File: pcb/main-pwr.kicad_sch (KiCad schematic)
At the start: 7 parts

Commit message: bom
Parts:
- C2: Part Description (none) -> CAP CER 0.1UF 16V X7R 0402
- R3, R5: Part Description (none) -> RES 10 OHM 1% 1/16W 0402
- R4: Part Description (none) -> WSKW0612 .003 1% EA E3
- R6, R7: footprint library:R_0402_1005Metric -> Resistor_SMD:R_0402_1005Metric; Manufacturer YAGEO -> Vishay Dale; Manufacturer Product Number RC0402FR-07100KL -> CRCW0402100KFKED; Part Description (none) -> RES 100K OHM 1% 1/16W 0402
- R8: renamed from R29; footprint library:R_0402_1005Metric -> Resistor_SMD:R_0402_1005Metric; Manufacturer YAGEO -> Vishay Dale; Manufacturer Product Number RC0402FR-07100KL -> CRCW0402100KFKED; Part Description (none) -> RES 100K OHM 1% 1/16W 0402
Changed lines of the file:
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@@
+			)
+		)
+		(property "Part Description" "RES 10 OHM 1% 1/16W 0402"
+			(at 45.72 31.75 0)
+			(effects
+				(font
+					(size 1.27 1.27)
+				)
+				(hide yes)
 			)
 		)
@@
 			)
 		)
-		(property "Footprint" "library:R_0402_1005Metric"
+		(property "Footprint" "Resistor_SMD:R_0402_1005Metric"
 			(at 128.524 62.484 90)
 			(effects
@@
 			)
 		)
-		(property "Manufacturer" "YAGEO"
+		(property "Manufacturer" "Vishay Dale"
 			(at 128.27 63.5 0)
 			(effects
@@
 			)
 		)
-		(property "Manufacturer Product Number" "RC0402FR-07100KL"
+		(property "Manufacturer Product Number" "CRCW0402100KFKED"
+			(at 128.27 63.5 90)
+			(effects
+				(font
+					(size 1.27 1.27)
+				)
+				(hide yes)
+			)
+		)
+		(property "Part Description" "RES 100K OHM 1% 1/16W 0402"
 			(at 128.27 63.5 90)
 			(effects
@@
 		(dnp no)
 		(fields_autoplaced yes)
-		(property "Reference" "R29"
+		(property "Reference" "R8"
 			(at 128.27 135.89 90)
 			(effects
@@
 			)
 		)
-		(property "Footprint" "library:R_0402_1005Metric"
+		(property "Footprint" "Resistor_SMD:R_0402_1005Metric"
 			(at 128.524 141.224 90)
 			(effects
@@
 			)
 		)
-		(property "Manufacturer" "YAGEO"
+		(property "Manufacturer" "Vishay Dale"
 			(at 128.27 142.24 0)
 			(effects
@@
 			)
 		)
-		(property "Manufacturer Product Number" "RC0402FR-07100KL"
+		(property "Manufacturer Product Number" "CRCW0402100KFKED"
+			(at 128.27 142.24 90)
+			(effects
+				(font
+					(size 1.27 1.27)
+				)
+				(hide yes)
+			)
+		)
+		(property "Part Description" "RES 100K OHM 1% 1/16W 0402"
 			(at 128.27 142.24 90)
 			(effects
@@
 			(project "RPi-HwAB-1"
 				(path "/e63e39d7-6ac0-4ffd-8aa3-1841a4541b55/f9ebb56c-78c7-42ac-bc19-ccbf788f5318"
-					(reference "R29")
+					(reference "R8")
 					(unit 1)
 				)
@@
 			)
 		)
+		(property "Part Description" "WSKW0612 .003 1% EA E3"
+			(at 39.37 25.4 90)
+			(effects
+				(font
+					(size 1.27 1.27)
+				)
+				(hide yes)
+			)
+		)
 		(pin "1"
 		)
@@
 		)
 		(property "Name" ""
+			(at 33.02 31.75 0)
+			(effects
+				(font
+					(size 1.27 1.27)
+				)
+				(hide yes)
+			)
+		)
+		(property "Part Description" "RES 10 OHM 1% 1/16W 0402"
 			(at 33.02 31.75 0)
 			(effects
@@
 			)
 		)
-		(property "Footprint" "library:R_0402_1005Metric"
+		(property "Footprint" "Resistor_SMD:R_0402_1005Metric"
 			(at 128.524 92.964 90)
 			(effects
@@
 			)
 		)
-		(property "Manufacturer" "YAGEO"
+		(property "Manufacturer" "Vishay Dale"
 			(at 128.27 93.98 0)
 			(effects
@@
 			)
 		)
-		(property "Manufacturer Product Number" "RC0402FR-07100KL"
+		(property "Manufacturer Product Number" "CRCW0402100KFKED"
+			(at 128.27 93.98 90)
+			(effects
+				(font
+					(size 1.27 1.27)
+				)
+				(hide yes)
+			)
+		)
+		(property "Part Description" "RES 100K OHM 1% 1/16W 0402"
 			(at 128.27 93.98 90)
 			(effects
@@
 			(at 39.37 40.64 90)
 			(effects
+				(font
+					(size 1.27 1.27)
+				)
+				(hide yes)
+			)
+		)
+		(property "Part Description" "CAP CER 0.1UF 16V X7R 0402"
+			(at 39.37 40.64 90)
+			(effects

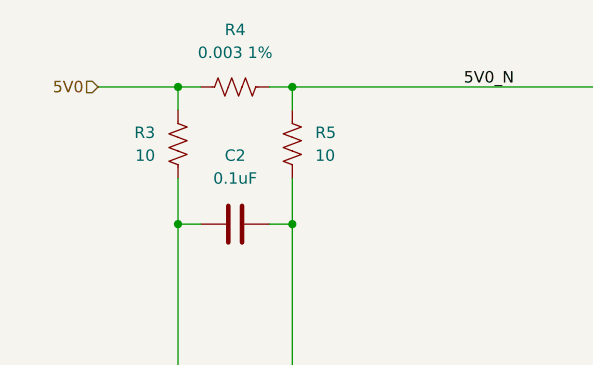
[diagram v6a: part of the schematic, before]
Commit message: added mig ddr pinout constraints
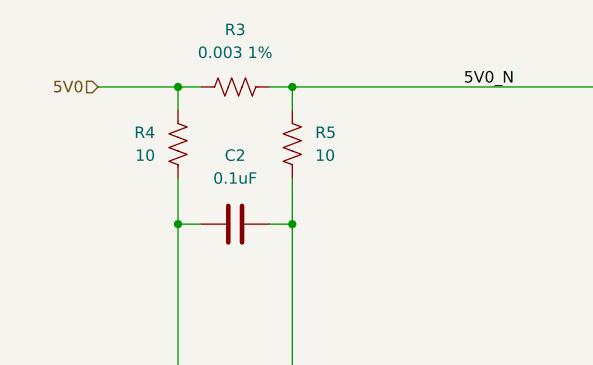
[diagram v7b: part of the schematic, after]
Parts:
- renumbered R4 to R3, R3 to R4
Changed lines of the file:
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@@
 		(dnp no)
 		(fields_autoplaced yes)
-		(property "Reference" "R4"
+		(property "Reference" "R3"
 			(at 39.37 19.05 90)
 			(effects
@@
 			(project ""
 				(path "/e63e39d7-6ac0-4ffd-8aa3-1841a4541b55/f9ebb56c-78c7-42ac-bc19-ccbf788f5318"
-					(reference "R4")
+					(reference "R3")
 					(unit 1)
 				)
@@
 		(on_board yes)
 		(dnp no)
-		(property "Reference" "R3"
+		(property "Reference" "R4"
 			(at 30.48 30.48 0)
 			(effects
@@
 			(project ""
 				(path "/e63e39d7-6ac0-4ffd-8aa3-1841a4541b55/f9ebb56c-78c7-42ac-bc19-ccbf788f5318"
-					(reference "R3")
+					(reference "R4")
 					(unit 1)
 				)

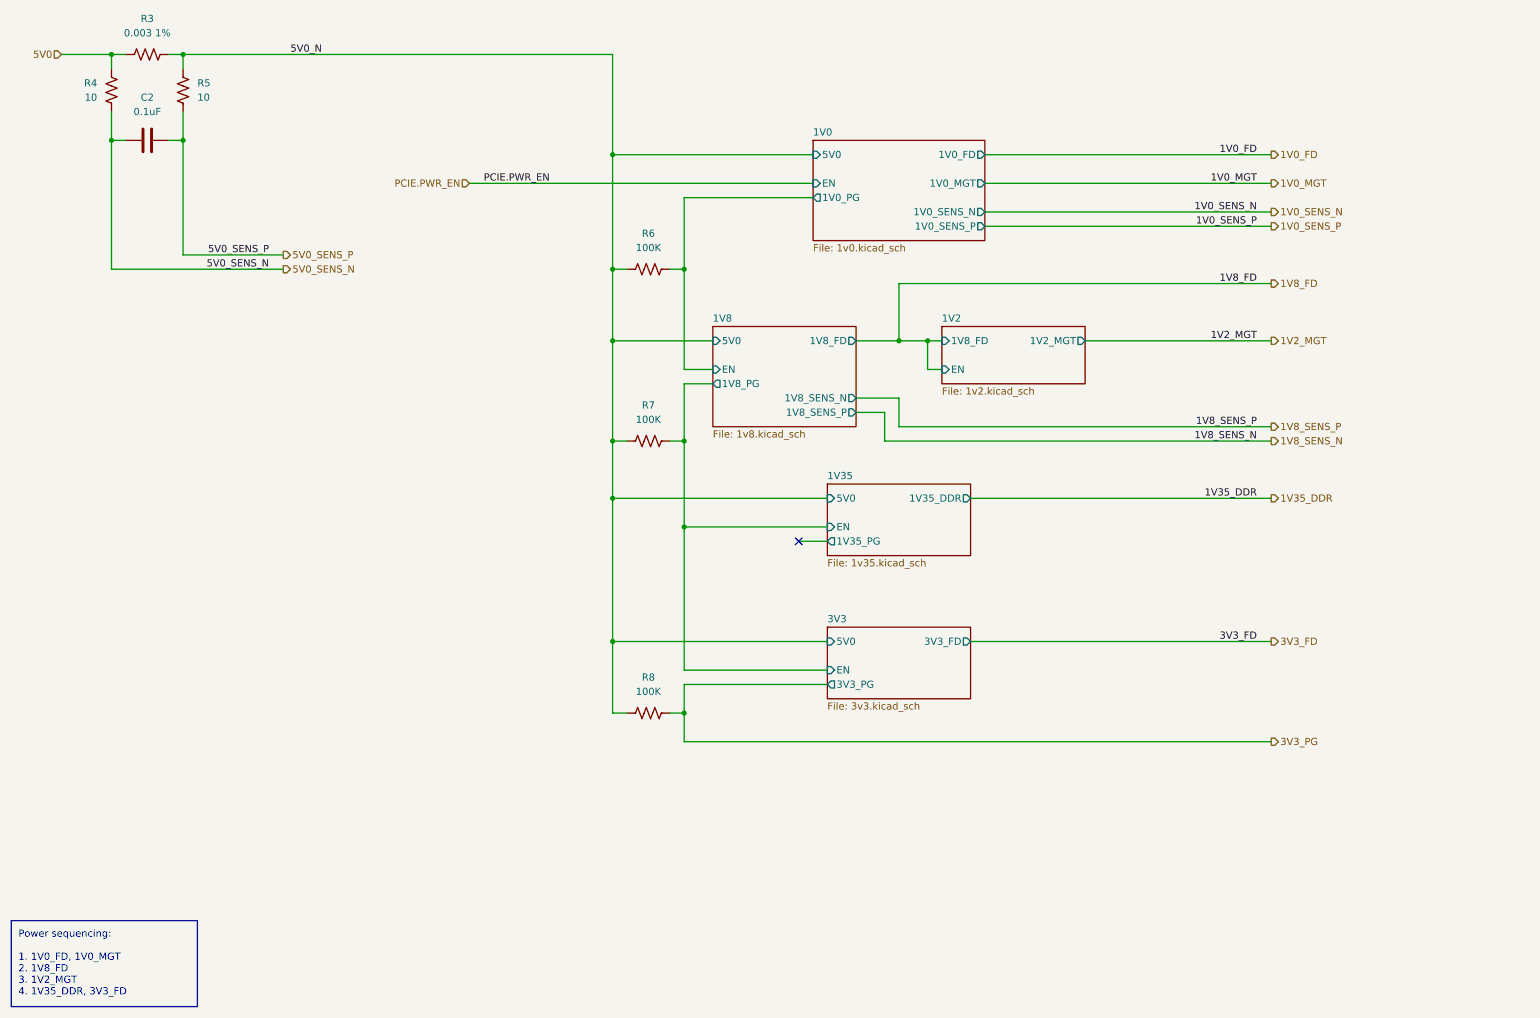
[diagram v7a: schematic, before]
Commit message: restructured power, power plane layout
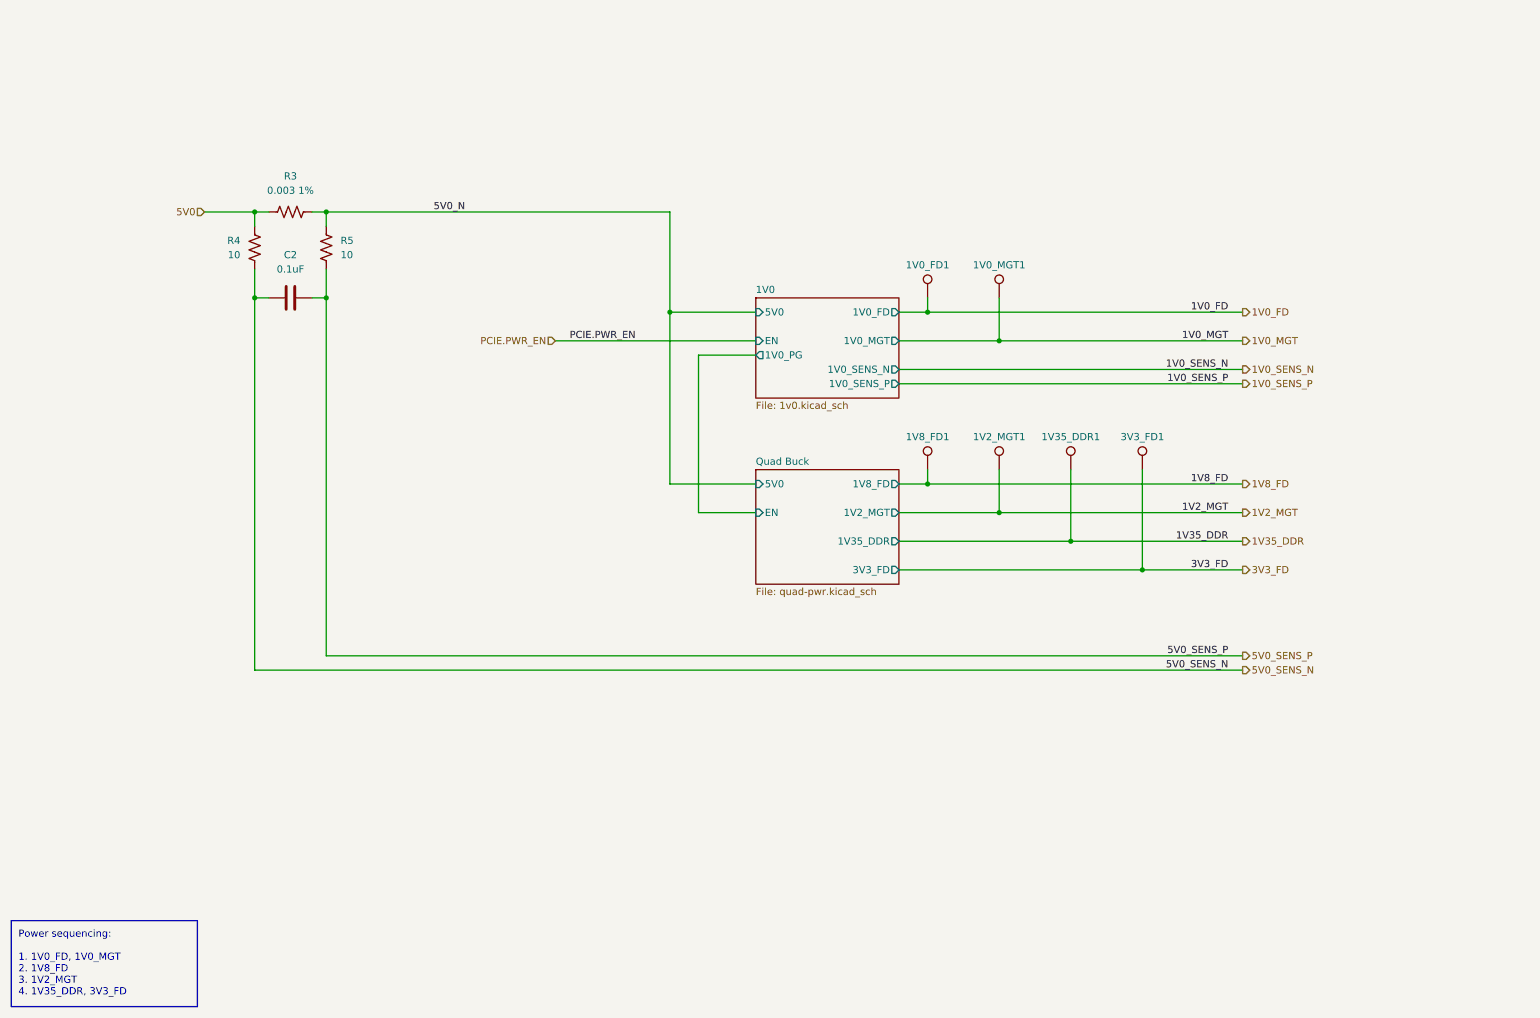
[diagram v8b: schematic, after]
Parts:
- removed R6, R7, R8: 100K, Resistor_SMD:R_0402_1005Metric, symbol library:R_US
- added 1V0_FD1, 1V0_MGT1, 1V2_MGT1, 1V35_DDR1, 1V8_FD1, 3V3_FD1: TestPoint, TestPoint:TestPoint_Pad_D1.0mm, symbol library:TestPoint
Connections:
- net 1V0_FD: now also 1V0_FD1.1
- net 1V0_MGT: now also 1V0_MGT1.1
- net 1V2_MGT: now also 1V2_MGT1.1
- net 1V35_DDR: now also 1V35_DDR1.1
- net 1V8_FD: now also 1V8_FD1.1
- net 3V3_FD: now also 3V3_FD1.1
- no-connect marks 1 -> 0
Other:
- removed sheet 1V2
- removed sheet 1V35
- removed sheet 1V8
- removed sheet 3V3
- added sheet Quad Buck (quad-pwr.kicad_sch)
- moved on the sheet: C2, R3, R4, R5
